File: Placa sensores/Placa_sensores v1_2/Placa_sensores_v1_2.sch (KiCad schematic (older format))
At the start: 64 parts, among them J1 Conn_02x08_Odd_Even, Q1 2n2222a, Q2 2n2222a, Q3 2n2222a, Q4 2n2222a, Q5 2n2222a, Q6 2n2222a, Q7 2n2222a, Q8 2n2222a, Q9 2n2222a, U1 TCRT5000, U2 TCRT5000, U3 TCRT5000, U4 TCRT5000, U5 TCRT5000, U6 TCRT5000, U7 TCRT5000, U8 TCRT5000, U9 TCRT5000

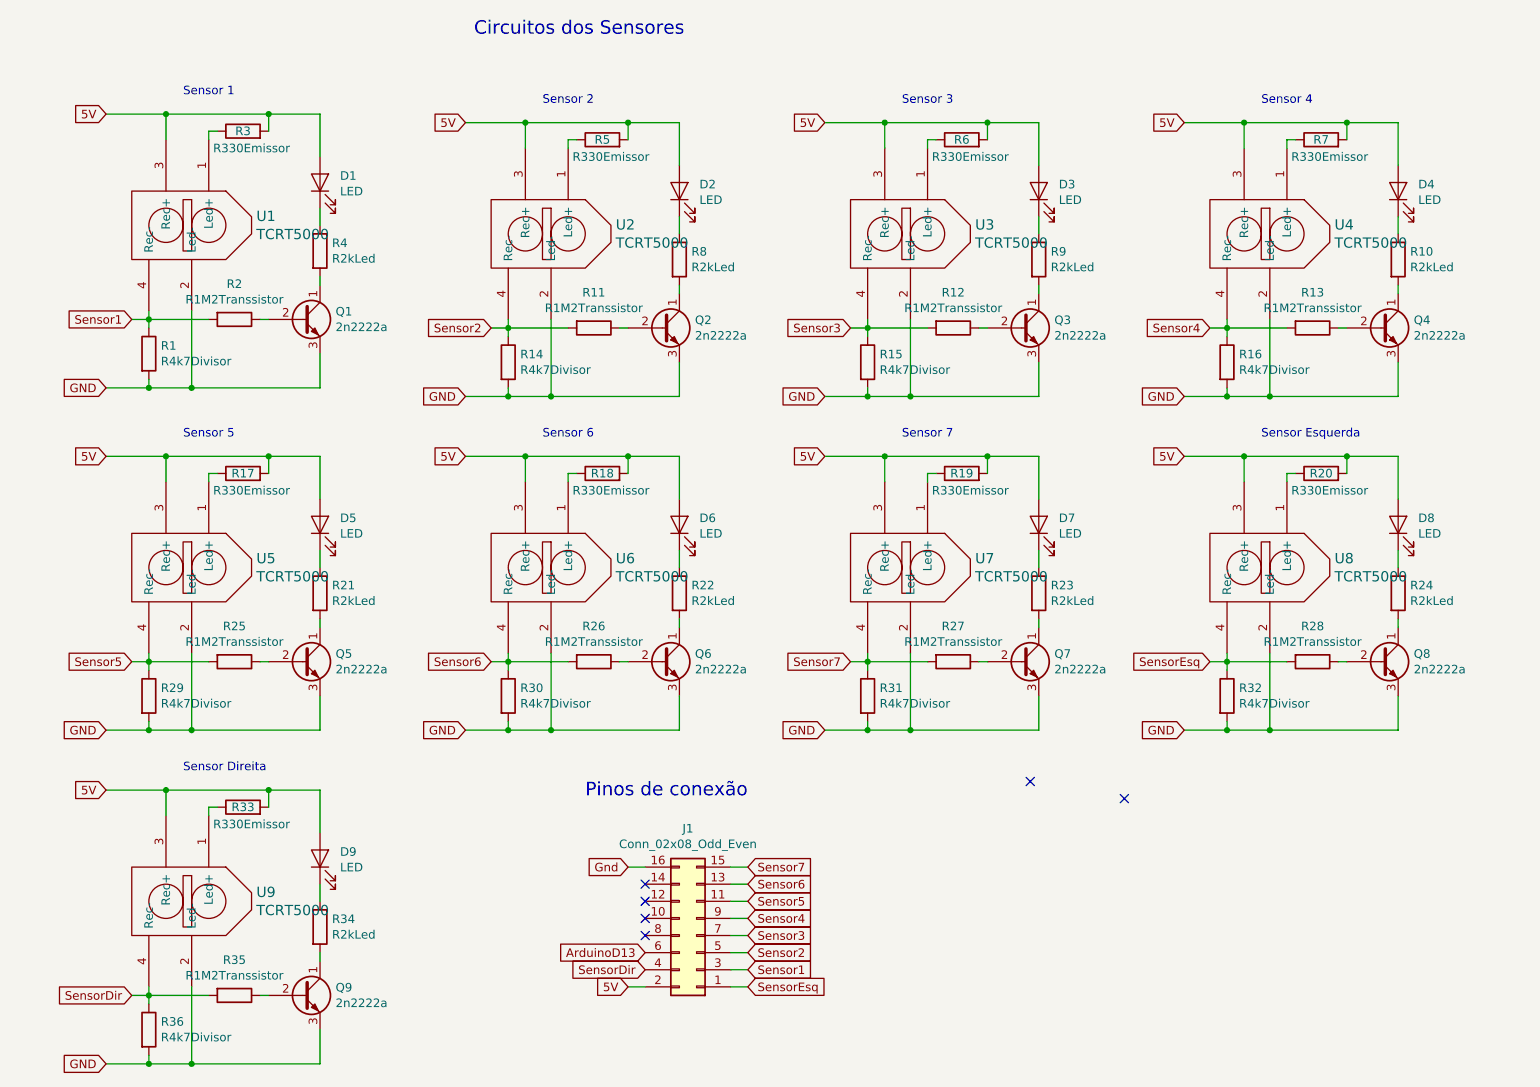
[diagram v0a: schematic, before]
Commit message: Continuação dos acertos finais
Foram acertadas as pastas e projetos da placa de sensores. Separando em dois projetos diferentes e ligando eles por um projeto hierárquico.
Falta para ser feito a da placa central e por fim, juntar tudo em um projeto só.
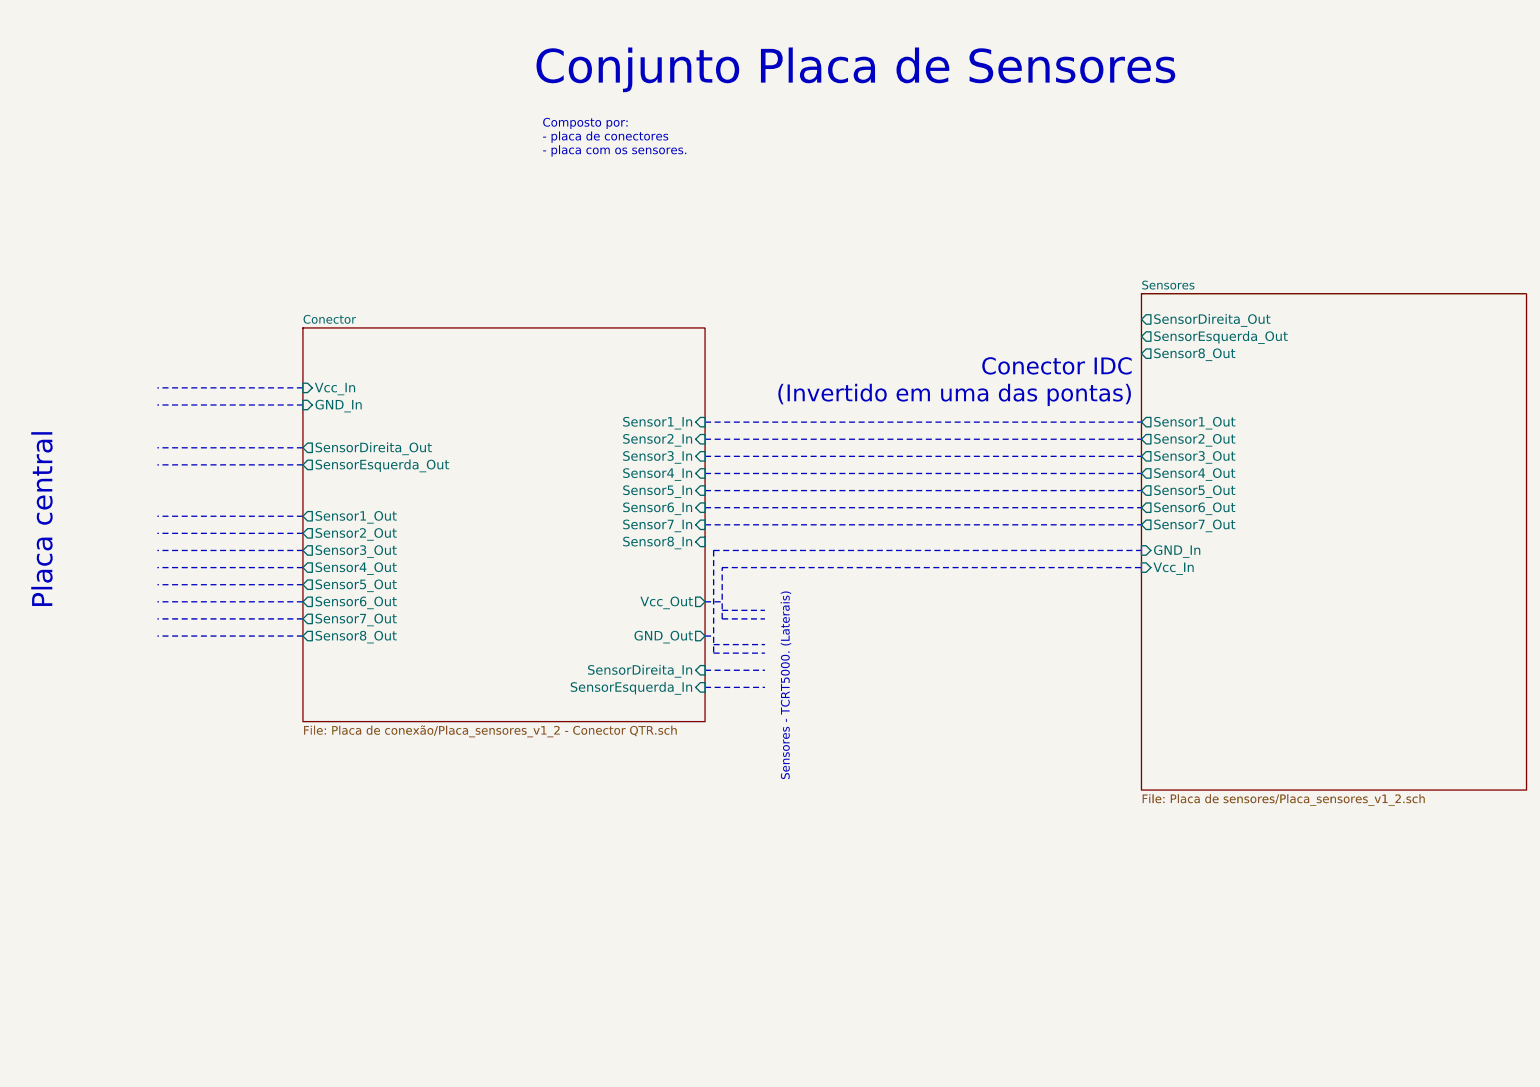
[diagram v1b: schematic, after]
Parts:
- removed D1, D2, D3, D4, D5, D6, D7, D8, D9: LED, LED_THT:LED_D3.0mm, symbol Device:LED
- removed J1: Conn_02x08_Odd_Even, Connector_IDC:IDC-Header_2x08_P2.54mm_Horizontal, symbol Connector_Generic:Conn_02x08_Odd_Even
- removed Q1, Q2, Q3, Q4, Q5, Q6, Q7, Q8, Q9: 2n2222a, Package_TO_SOT_THT:TO-92_Wide, symbol Transistor_BJT:BC338
- removed R1, R14, R15, R16, R29, R30, R31, R32, R36: R4k7Divisor, Resistor_THT:R_Axial_DIN0207_L6.3mm_D2.5mm_P10.16mm_Horizontal, symbol Device:R
- removed R10, R21, R22, R23, R24, R34, R4, R8, R9: R2kLed, Resistor_THT:R_Axial_DIN0207_L6.3mm_D2.5mm_P10.16mm_Horizontal, symbol Device:R
- removed R11, R12, R13, R2, R25, R26, R27, R28, R35: R1M2Transsistor, Resistor_THT:R_Axial_DIN0207_L6.3mm_D2.5mm_P10.16mm_Horizontal, symbol Device:R
- removed R17, R18, R19, R20, R3, R33, R5, R6, R7: R330Emissor, Resistor_THT:R_Axial_DIN0207_L6.3mm_D2.5mm_P10.16mm_Horizontal, symbol Device:R
- removed U1, U2, U3, U4, U5, U6, U7, U8, U9: TCRT5000, Sensores_SL:TCRT5000Extendido, symbol Sensores_SL:TCRT5000
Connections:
- no-connect marks 6 -> 0
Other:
- note added: "Composto por: \n- placa de conectores \n- placa com os sensores."
- note added: "Conector IDC \n(Invertido em uma das pontas)"
- note added: "Conjunto Placa de Sensores"
- note added: "Placa central"
- note added: "Sensores - TCRT5000. (Laterais)"
- note removed: "Circuitos dos Sensores"
- note removed: "Pinos de conexão"
- note removed: "Sensor 1"
- note removed: "Sensor 2"
- note removed: "Sensor 3"
- note removed: "Sensor 4"
- note removed: "Sensor 5"
- note removed: "Sensor 6"
- note removed: "Sensor 7"
- note removed: "Sensor Direita"
- note removed: "Sensor Esquerda"

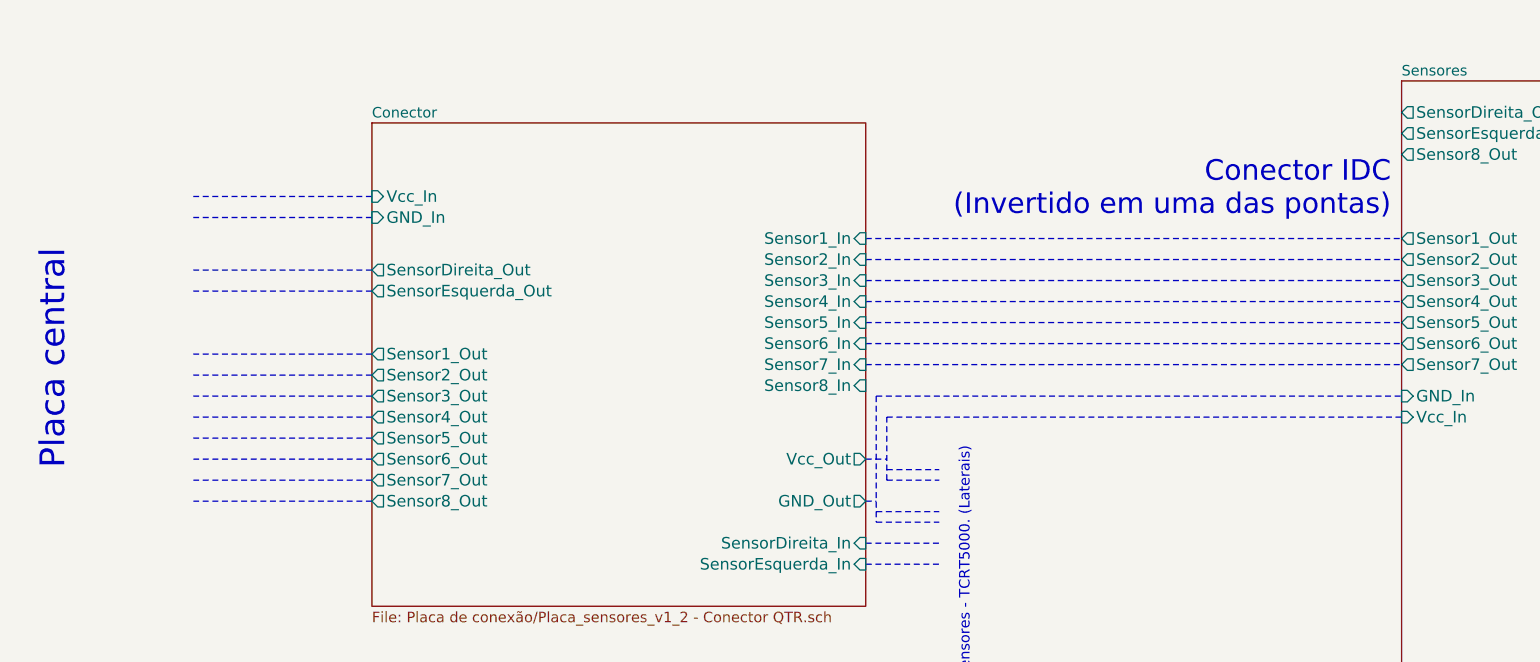
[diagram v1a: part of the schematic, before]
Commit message: Ajuste final
Acertado a placa central, verificado conflitos de etiquetas hierárquicas, ligados os projeto um no outro, ajustado o projeto principal e linkado todos as placas ao projeto principal.
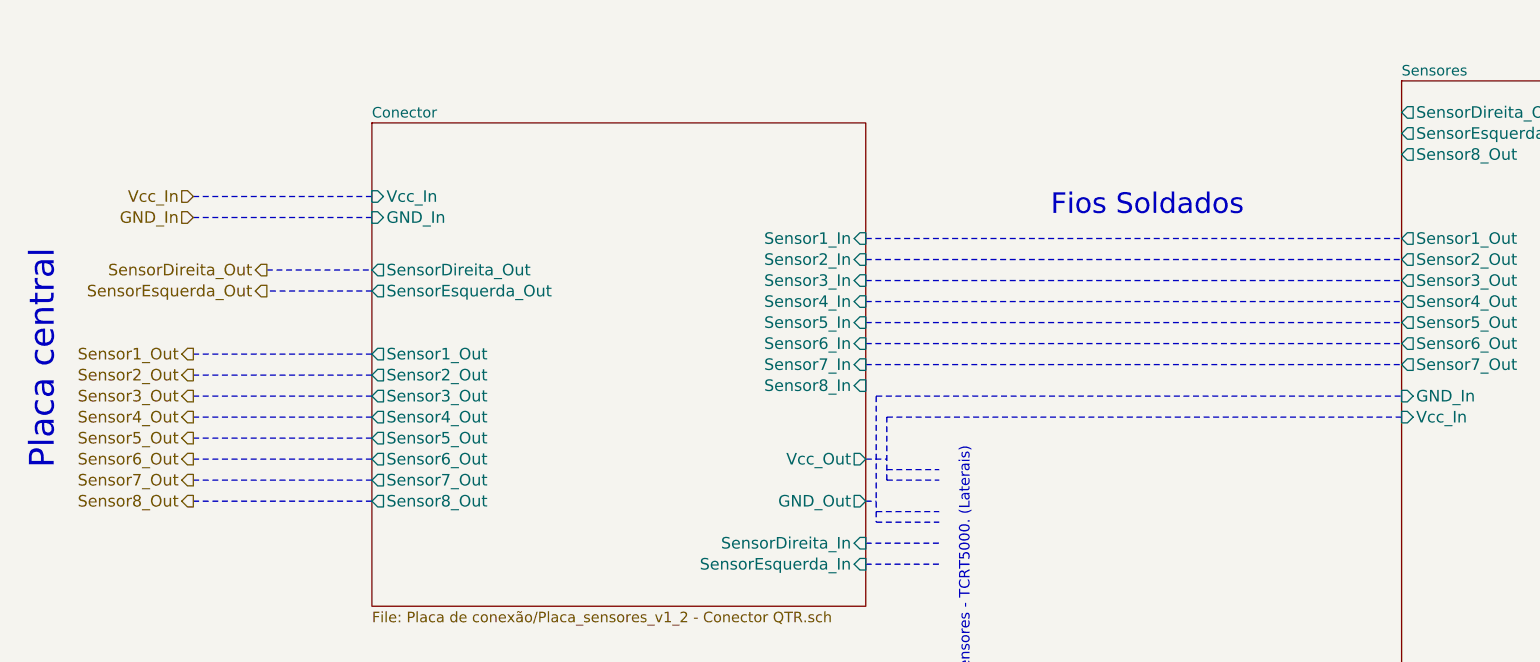
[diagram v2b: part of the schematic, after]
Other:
- note added: "Fios Soldados"
- note removed: "Conector IDC \n(Invertido em uma das pontas)"
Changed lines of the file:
@@
 $Descr A4 11693 8268
 encoding utf-8
-Sheet 1 3
+Sheet 4 7
 Title ""
 Date ""
@@
 Comment4 ""
 $EndDescr
-$Sheet
-S 7350 2350 2250 2900
-U 5E5A3DFE
-F0 "Sensores" 50
-F1 "Placa de sensores/Placa_sensores_v1_2.sch" 50
-F2 "Vcc_In" I L 7350 3950 55
-F3 "GND_In" I L 7350 3850 55
-F4 "SensorDireita_Out" O L 7350 2500 55
-F5 "SensorEsquerda_Out" O L 7350 2600 55
-F6 "Sensor1_Out" O L 7350 3100 55
-F7 "Sensor2_Out" O L 7350 3200 55
-F8 "Sensor3_Out" O L 7350 3300 55
-F9 "Sensor4_Out" O L 7350 3400 55
-F10 "Sensor5_Out" O L 7350 3500 55
-F11 "Sensor6_Out" O L 7350 3600 55
-F12 "Sensor7_Out" O L 7350 3700 55
-F13 "Sensor8_Out" O L 7350 2700 55
-$EndSheet
 Text Notes 3800 1150 0    197  ~ 0
 Conjunto Placa de Sensores
 Text Notes 3850 1550 0    50   ~ 0
 Composto por: \n- placa de conectores \n- placa com os sensores.
-Text Notes 1000 4200 1    118  ~ 0
+Text Notes 950  4200 1    118  ~ 0
 Placa central
-Text Notes 7300 3000 2    98   ~ 0
-            Conector IDC \n(Invertido em uma das pontas)
-$Sheet
-S 2450 2550 2350 2300
-U 5E5895C4
-F0 "Conector" 50
-F1 "Placa de conexão/Placa_sensores_v1_2 - Conector QTR.sch" 50
-F2 "Vcc_In" I L 2450 2900 55
-F3 "GND_In" I L 2450 3000 55
-F4 "SensorDireita_Out" O L 2450 3250 55
-F5 "SensorEsquerda_Out" O L 2450 3350 55
-F6 "Sensor1_Out" O L 2450 3650 55
-F7 "Sensor2_Out" O L 2450 3750 55
-F8 "Sensor3_Out" O L 2450 3850 55
-F9 "Sensor4_Out" O L 2450 3950 55
-F10 "Sensor5_Out" O L 2450 4050 55
-F11 "Sensor6_Out" O L 2450 4150 55
-F12 "Sensor7_Out" O L 2450 4250 55
-F13 "Sensor8_Out" O L 2450 4350 55
-F14 "Vcc_Out" O R 4800 4150 55
-F15 "GND_Out" O R 4800 4350 55
-F16 "SensorDireita_In" I R 4800 4550 55
-F17 "SensorEsquerda_In" I R 4800 4650 55
-F18 "Sensor1_In" I R 4800 3100 55
-F19 "Sensor2_In" I R 4800 3200 55
-F20 "Sensor3_In" I R 4800 3300 55
-F21 "Sensor4_In" I R 4800 3400 55
-F22 "Sensor5_In" I R 4800 3500 55
-F23 "Sensor6_In" I R 4800 3600 55
-F24 "Sensor7_In" I R 4800 3700 55
-F25 "Sensor8_In" I R 4800 3800 55
-$EndSheet
+Text Notes 6600 3000 2    98   ~ 0
+Fios Soldados
 Text Notes 5300 5200 1    50   ~ 0
 Sensores - TCRT5000. (Laterais)
@@
 Wire Notes Line
 	2450 2900 1600 2900
-Wire Notes Line
-	2450 3350 1600 3350
-Wire Notes Line
-	2450 3250 1600 3250
 Wire Notes Line
 	4800 4350 4850 4350
@@
 Wire Notes Line
 	4900 3950 7350 3950
+$Sheet
+S 2450 2550 2350 2300
+U 5E5895C4
+F0 "Conector" 50
+F1 "Placa de conexão/Placa_sensores_v1_2 - Conector QTR.sch" 50
+F2 "Vcc_In" I L 2450 2900 55
+F3 "GND_In" I L 2450 3000 55
+F4 "SensorDireita_Out" O L 2450 3250 55
+F5 "SensorEsquerda_Out" O L 2450 3350 55
+F6 "Sensor1_Out" O L 2450 3650 55
+F7 "Sensor2_Out" O L 2450 3750 55
+F8 "Sensor3_Out" O L 2450 3850 55
+F9 "Sensor4_Out" O L 2450 3950 55
+F10 "Sensor5_Out" O L 2450 4050 55
+F11 "Sensor6_Out" O L 2450 4150 55
+F12 "Sensor7_Out" O L 2450 4250 55
+F13 "Sensor8_Out" O L 2450 4350 55
+F14 "Vcc_Out" O R 4800 4150 55
+F15 "GND_Out" O R 4800 4350 55
+F16 "SensorDireita_In" I R 4800 4550 55
+F17 "SensorEsquerda_In" I R 4800 4650 55
+F18 "Sensor1_In" I R 4800 3100 55
+F19 "Sensor2_In" I R 4800 3200 55
+F20 "Sensor3_In" I R 4800 3300 55
+F21 "Sensor4_In" I R 4800 3400 55
+F22 "Sensor5_In" I R 4800 3500 55
+F23 "Sensor6_In" I R 4800 3600 55
+F24 "Sensor7_In" I R 4800 3700 55
+F25 "Sensor8_In" I R 4800 3800 55
+$EndSheet
+$Sheet
+S 7350 2350 2250 2900
+U 5E5A3DFE
+F0 "Sensores" 50
+F1 "Placa de sensores/Placa_sensores_v1_2.sch" 50
+F2 "Vcc_In" I L 7350 3950 55
+F3 "GND_In" I L 7350 3850 55
+F4 "SensorDireita_Out" O L 7350 2500 55
+F5 "SensorEsquerda_Out" O L 7350 2600 55
+F6 "Sensor1_Out" O L 7350 3100 55
+F7 "Sensor2_Out" O L 7350 3200 55
+F8 "Sensor3_Out" O L 7350 3300 55
+F9 "Sensor4_Out" O L 7350 3400 55
+F10 "Sensor5_Out" O L 7350 3500 55
+F11 "Sensor6_Out" O L 7350 3600 55
+F12 "Sensor7_Out" O L 7350 3700 55
+F13 "Sensor8_Out" O L 7350 2700 55
+$EndSheet
+Text HLabel 1600 2900 0    55   Input ~ 0
+Vcc_In
+Text HLabel 1600 3000 0    55   Input ~ 0
+GND_In
+Text HLabel 1950 3250 0    55   Output ~ 0
+SensorDireita_Out
+Text HLabel 1950 3350 0    55   Output ~ 0
+SensorEsquerda_Out
+Text HLabel 1600 3650 0    55   Output ~ 0
+Sensor1_Out
+Text HLabel 1600 3750 0    55   Output ~ 0
+Sensor2_Out
+Text HLabel 1600 3850 0    55   Output ~ 0
+Sensor3_Out
+Text HLabel 1600 3950 0    55   Output ~ 0
+Sensor4_Out
+Text HLabel 1600 4050 0    55   Output ~ 0
+Sensor5_Out
+Text HLabel 1600 4150 0    55   Output ~ 0
+Sensor6_Out
+Text HLabel 1600 4250 0    55   Output ~ 0
+Sensor7_Out
+Text HLabel 1600 4350 0    55   Output ~ 0
+Sensor8_Out
+Wire Notes Line
+	1950 3250 2450 3250
+Wire Notes Line
+	2450 3350 1950 3350
 $EndSCHEMATC
